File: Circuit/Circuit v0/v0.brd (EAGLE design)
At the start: 106.7 x 94 mm, 10 parts, among them U1 CD4051BE, U2 CD4051BE

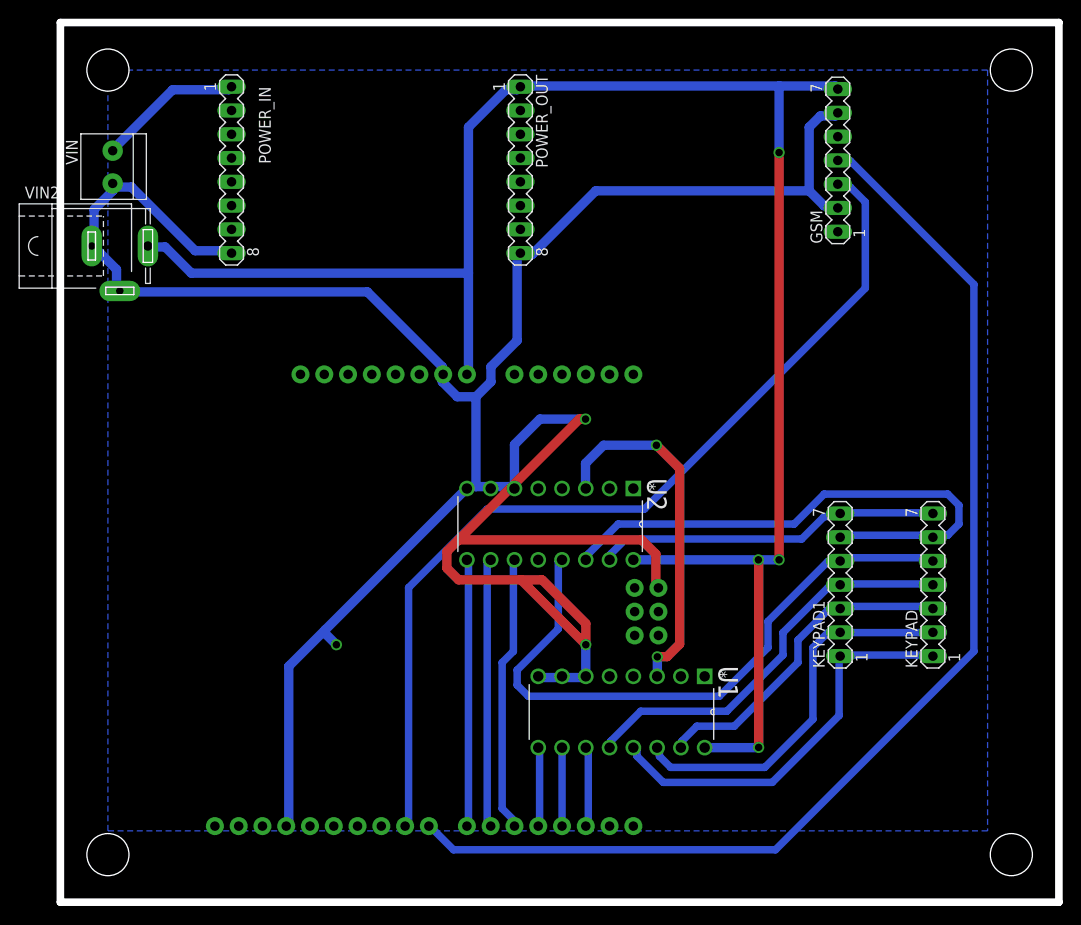
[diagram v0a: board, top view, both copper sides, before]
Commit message: v0 smaller and removed KiCAD files
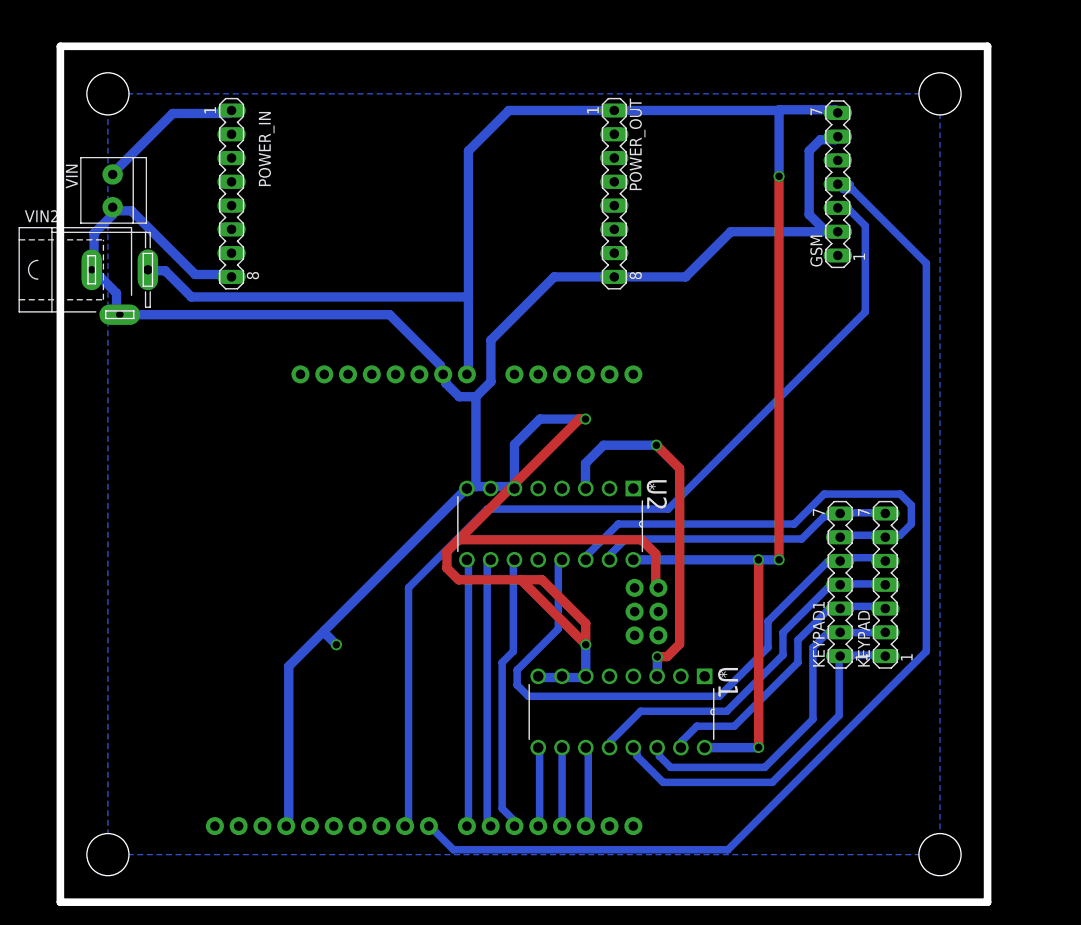
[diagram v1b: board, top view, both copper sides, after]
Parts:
- moved POWER_OUT 10.3 mm to (59.2, 75.7)
- moved KEYPAD 5.08 mm to (88.1, 33.9)
- moved GSM 2.54 mm to (83.1, 76.7)
- moved POWER_IN 2.54 mm to (18.3, 75.7)
- moved VIN 2.54 mm to (5.59, 75.9)
- moved VIN2 2.54 mm to (6.35, 67.6)
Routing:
- net COL2: track 59.0 -> 48.8 mm
- net TX: track 127.3 -> 118.7 mm
- net VCC: track 195.5 -> 190.4 mm
- net COL1: track 68.5 -> 63.4 mm
- net COL3: track 37.0 -> 32.0 mm
- net ROW4: track 43.6 -> 38.6 mm
- net ROW2: track 41.3 -> 36.2 mm
- net ROW1: track 43.3 -> 38.2 mm
- net ROW3: track 35.1 -> 30.0 mm
- net GND: track 299.2 -> 297.0 mm
- net RX: track 100.7 -> 99.6 mm
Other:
- board size 106.7 x 94 mm -> 99.1 x 91.4 mm

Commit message: circuit for fabrication
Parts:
- POWER_IN, POWER_OUT: device con-lstb:MA08-1 -> con-lstb:MA08-2
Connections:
- new net P13: POWER_IN.3, POWER_IN.4
- new net P14: POWER_IN.5, POWER_IN.6
- new net P15: POWER_IN.7, POWER_IN.8
- new net P16: POWER_IN.10, POWER_IN.9
- new net P17: POWER_IN.11, POWER_IN.12
- new net P18: POWER_IN.13, POWER_IN.14
- new net P23: POWER_OUT.3, POWER_OUT.4
- new net P24: POWER_OUT.5, POWER_OUT.6
- new net P25: POWER_OUT.7, POWER_OUT.8
- new net P26: POWER_OUT.10, POWER_OUT.9
- new net P27: POWER_OUT.11, POWER_OUT.12
- new net P28: POWER_OUT.13, POWER_OUT.14
- net 12V: now also POWER_IN.2
- net GND: now also POWER_IN.15, POWER_IN.16, POWER_OUT.15, POWER_OUT.16; no longer POWER_IN.8, POWER_OUT.8
- net VCC: now also POWER_OUT.2
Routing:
- net GND: track 297.0 -> 221.1 mm
- net VCC: track 190.4 -> 129.3 mm
- net COM: track 38.4 -> 13.2 mm
- net P28: track 0.00 -> 2.54 mm
- net P27: track 0.00 -> 2.54 mm
- net P26: track 0.00 -> 2.54 mm
- net P25: track 0.00 -> 2.54 mm
- net P24: track 0.00 -> 2.54 mm
- net P23: track 0.00 -> 2.54 mm
- net P18: track 0.00 -> 2.54 mm
- net P17: track 0.00 -> 2.54 mm
- net P16: track 0.00 -> 2.54 mm
- net P15: track 0.00 -> 2.54 mm
- net P14: track 0.00 -> 2.54 mm
- net P13: track 0.00 -> 2.54 mm
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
